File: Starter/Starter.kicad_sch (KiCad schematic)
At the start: 62 parts, among them J2 Speaker, J5 Conn_01x08_Pin, M1 Vibration Motor, Q1 2N2222, SW1 UP, SW2 LEFT, SW3 DOWN, SW4 RIGHT, U2 LP-MSPM0G3507, U3 MCP34119D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

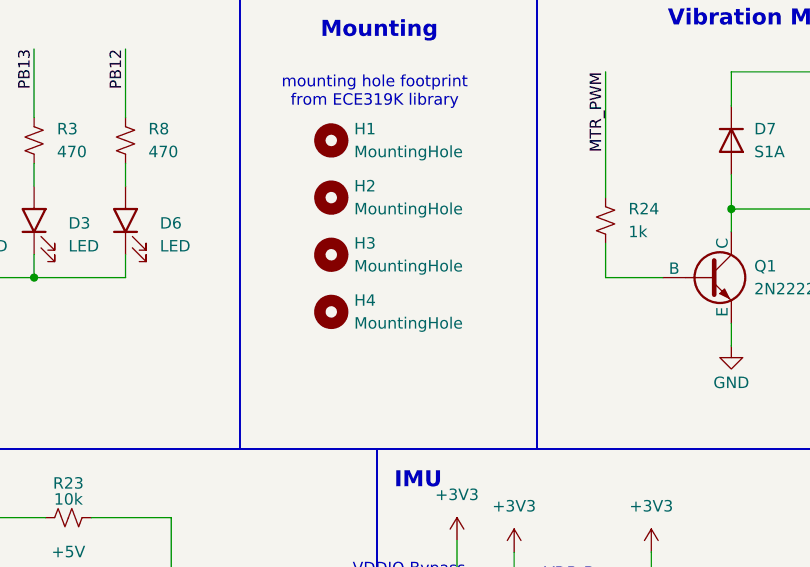
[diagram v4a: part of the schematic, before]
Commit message: Component placements finalized
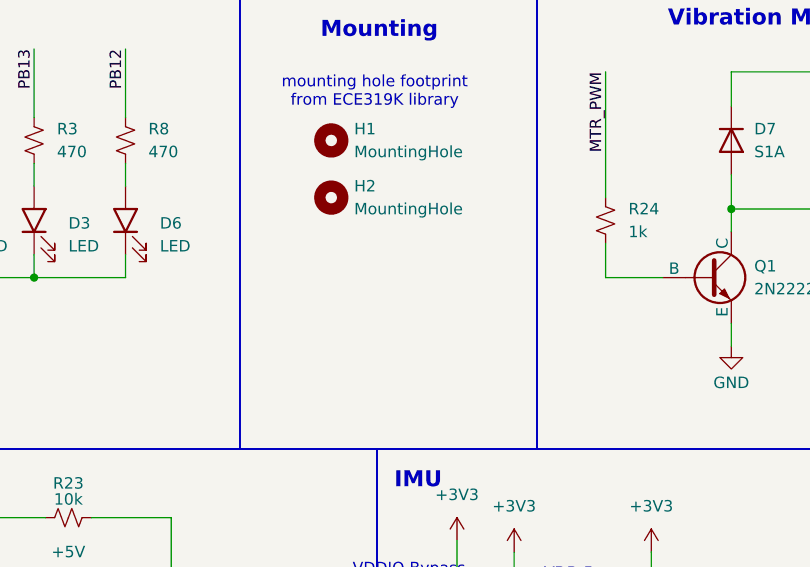
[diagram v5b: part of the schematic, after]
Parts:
- removed H3, H4: MountingHole, MountingHole:MountingHole_3.2mm_M3, symbol Mechanical:MountingHole
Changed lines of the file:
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@@
 	)
 	(symbol
-		(lib_id "Mechanical:MountingHole")
-		(at 261.62 156.21 0)
-		(unit 1)
-		(exclude_from_sim no)
-		(in_bom no)
-		(on_board yes)
-		(dnp no)
-		(fields_autoplaced yes)
-		(property "Reference" "H4"
-			(at 264.16 154.9399 0)
-			(effects
-				(font
-					(size 1.27 1.27)
-				)
-				(justify left)
-			)
-		)
-		(property "Value" "MountingHole"
-			(at 264.16 157.4799 0)
-			(effects
-				(font
-					(size 1.27 1.27)
-				)
-				(justify left)
-			)
-		)
-		(property "Footprint" "MountingHole:MountingHole_3.2mm_M3"
-			(at 261.62 156.21 0)
-			(effects
-				(font
-					(size 1.27 1.27)
-				)
-				(hide yes)
-			)
-		)
-		(property "Datasheet" "~"
-			(at 261.62 156.21 0)
-			(effects
-				(font
-					(size 1.27 1.27)
-				)
-				(hide yes)
-			)
-		)
-		(property "Description" "Mounting Hole without connection"
-			(at 261.62 156.21 0)
-			(effects
-				(font
-					(size 1.27 1.27)
-				)
-				(hide yes)
-			)
-		)
-		(property "Mouser Link" ""
-			(at 261.62 156.21 0)
-			(effects
-				(font
-					(size 1.27 1.27)
-				)
-				(hide yes)
-			)
-		)
-		(property "Mouser #" ""
-			(at 261.62 156.21 0)
-			(effects
-				(font
-					(size 1.27 1.27)
-				)
-				(hide yes)
-			)
-		)
-		(property "JLCPCB #" ""
-			(at 261.62 156.21 0)
-			(effects
-				(font
-					(size 1.27 1.27)
-				)
-				(hide yes)
-			)
-		)
-		(instances
-			(project "Starter"
-				(path "/69b823fd-c065-40ff-9bb9-c5835555f3eb"
-					(reference "H4")
-					(unit 1)
-				)
-			)
-		)
-	)
-	(symbol
 		(lib_id "ECE319K:C")
 		(at 212.09 205.74 270)
@@
 					(unit 1)
 				)
-			)
-		)
-	)
-	(symbol
-		(lib_id "Mechanical:MountingHole")
-		(at 261.62 149.86 0)
-		(unit 1)
-		(exclude_from_sim no)
-		(in_bom no)
-		(on_board yes)
-		(dnp no)
-		(fields_autoplaced yes)
-		(property "Reference" "H3"
-			(at 264.16 148.5899 0)
-			(effects
-				(font
-					(size 1.27 1.27)
-				)
-				(justify left)
-			)
-		)
-		(property "Value" "MountingHole"
-			(at 264.16 151.1299 0)
-			(effects
-				(font
-					(size 1.27 1.27)
-				)
-				(justify left)
-			)
-		)
-		(property "Footprint" "MountingHole:MountingHole_3.2mm_M3"
-			(at 261.62 149.86 0)
-			(effects
-				(font
-					(size 1.27 1.27)
-				)
-				(hide yes)
-			)
-		)
-		(property "Datasheet" "~"
-			(at 261.62 149.86 0)
-			(effects
-				(font
-					(size 1.27 1.27)
-				)
-				(hide yes)
-			)
-		)
-		(property "Description" "Mounting Hole without connection"
-			(at 261.62 149.86 0)
-			(effects
-				(font
-					(size 1.27 1.27)
-				)
-				(hide yes)
-			)
-		)
-		(property "Mouser Link" ""
-			(at 261.62 149.86 0)
-			(effects
-				(font
-					(size 1.27 1.27)
-				)
-				(hide yes)
-			)
-		)
-		(property "Mouser #" ""
-			(at 261.62 149.86 0)
-			(effects
-				(font
-					(size 1.27 1.27)
-				)
-				(hide yes)
-			)
-		)
-		(property "JLCPCB #" ""
-			(at 261.62 149.86 0)
-			(effects
-				(font
-					(size 1.27 1.27)
-				)
-				(hide yes)
-			)
-		)
-		(instances
-			(project "Starter"
-				(path "/69b823fd-c065-40ff-9bb9-c5835555f3eb"
-					(reference "H3")
-					(unit 1)
-				)

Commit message: final board! ordered
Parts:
- removed J5: Conn_01x08_Pin, Connector_PinSocket_2.54mm:PinSocket_1x08_P2.54mm_Vertical, symbol Connector:Conn_01x08_Pin
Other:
- note removed: "Extra"
- note removed: "break out any remaining pins here"

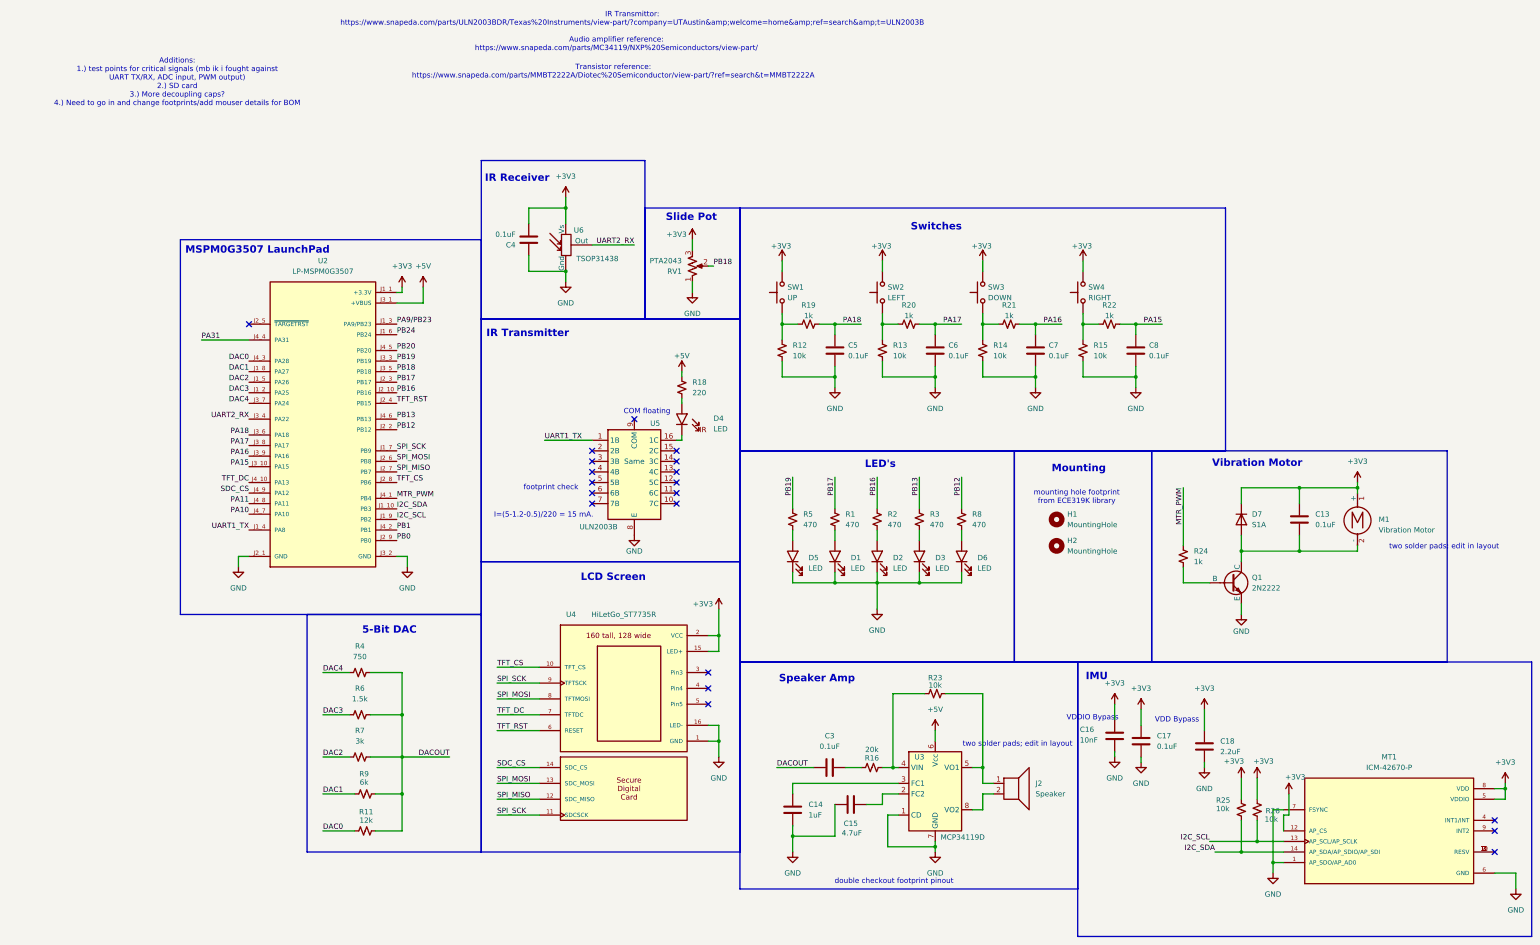
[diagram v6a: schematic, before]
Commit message: all mouser links attached
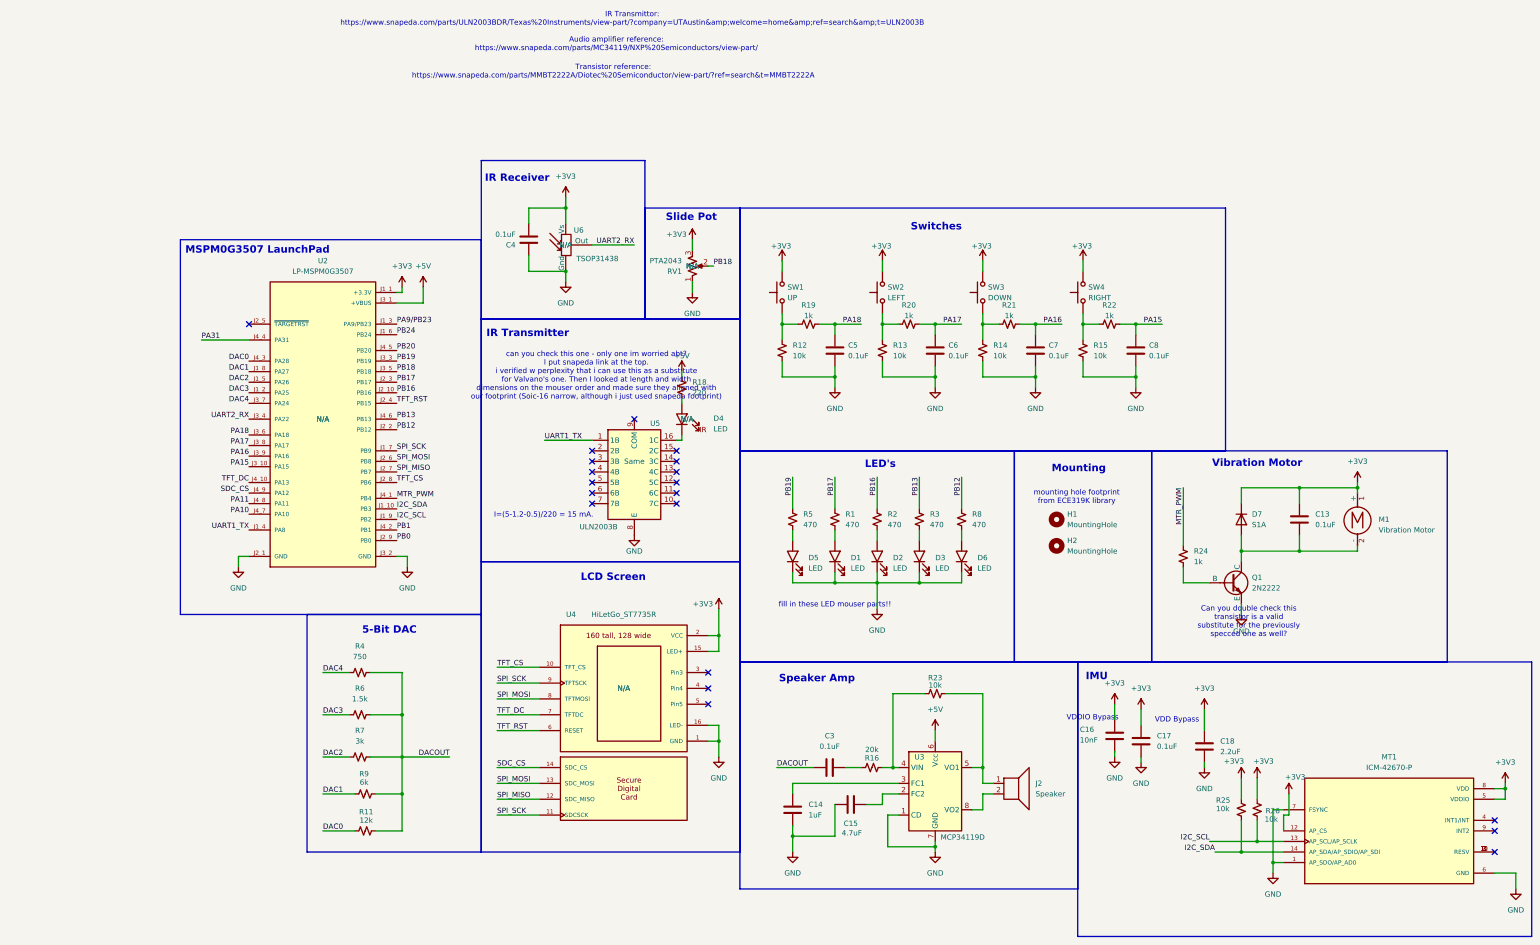
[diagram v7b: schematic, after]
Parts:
- C13, C17, C3, C4, C5, C6, C7, C8: Mouser # (none) -> 581-0603ZG104ZAT2A; Mouser Link (none) -> https://www.mouser.com/ProductDetail/KYOCERA-AVX/0603ZG104Z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
- C14: Mouser # (none) -> 963-LMK107B7105KA-T; Mouser Link (none) -> https://www.mouser.com/ProductDetail/TAIYO-YUDEN/LMK107B710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
- C15: Mouser # (none) -> 963-LMK107BJ475KA-T; Mouser Link (none) -> https://www.mouser.com/ProductDetail/TAIYO-YUDEN/LMK107BJ47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
- C16: Mouser # (none) -> 581-0603ZC103MAT2A; Mouser Link (none) -> https://www.mouser.com/ProductDetail/KYOCERA-AVX/0603ZC103M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
- C18: Mouser # (none) -> 963-LMK107BJ225KA-T; Mouser Link (none) -> https://www.mouser.com/ProductDetail/TAIYO-YUDEN/LMK107BJ22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
- D4, J2, RV1, U2, U3, U4, U6: Mouser # (none) -> N/A; Mouser Link (none) -> N/A
- M1: Mouser # 316040001 -> 713-316040001
- R1, R2, R3, R5, R8: Mouser # (none) -> 71-CRCW0603-470-E3; Mouser Link (none) -> https://www.mouser.com/ProductDetail/Vishay-Dale/CRCW060347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
- R11: Mouser # (none) -> 71-CRCW0603-12K-E3; Mouser Link (none) -> https://www.mouser.com/ProductDetail/Vishay-Dale/CRCW060312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
- R12, R13, R14, R15, R23, R25, R26: Mouser # (none) -> 71-CRCW060310K0FKEC; Mouser Link (none) -> https://www.mouser.com/ProductDetail/Vishay-Dale/CRCW060310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
- R16: Mouser # (none) -> 71-CRCW0603-20K-E3; Mouser Link (none) -> https://www.mouser.com/ProductDetail/Vishay-Dale/CRCW060320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
- R18: Mouser # (none) -> 71-CRCW0603-220-E3; Mouser Link (none) -> https://www.mouser.com/ProductDetail/Vishay-Dale/CRCW060322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
- R19, R20, R21, R22, R24: Mouser # (none) -> 71-CRCW06031K00FKEC; Mouser Link (none) -> https://www.mouser.com/ProductDetail/Vishay-Dale/CRCW06031K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
- R4: Mouser # (none) -> 71-CRCW0603-750-E3; Mouser Link (none) -> https://www.mouser.com/ProductDetail/Vishay-Dale/CRCW060375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
- R6: Mouser # (none) -> 71-CRCW06031K50FKEC; Mouser Link (none) -> https://www.mouser.com/ProductDetail/Vishay-Dale/CRCW06031K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
- R7: Mouser # (none) -> 71-CRCW0603-3K-E3; Mouser Link (none) -> https://www.mouser.com/ProductDetail/Vishay-Dale/CRCW06033K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
- R9: Mouser # (none) -> 71-CRCW0603-6.04K-E3; Mouser Link (none) -> https://www.mouser.com/ProductDetail/Vishay-Dale/CRCW06036K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
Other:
- note added: "Can you double check this transistor is a valid substitute for the previously specced one as well?"
- note added: "can you check this one - only one im worried abt? I put snapeda link at the top. i verified w perplexity that i can use this as a substitute for Valvano's one. Then I looked at length and width dimensions on the mouser order and made sure they aligned with our footprint (Soic-16 narrow, although i just used snapeda footprint)"
- note added: "fill in these LED mouser parts!!"
- note removed: "Additions: 1.) test points for critical signals (mb ik i fought against UART TX/RX, ADC input, PWM output) 2.) SD card 3.) More decoupling caps? 4.) Need to go in and change footprints/add mouser details for BOM"
- note removed: "COM floating"
- note removed: "double checkout footprint pinout"
- note removed: "footprint check"
- note removed: "two solder pads; edit in layout"

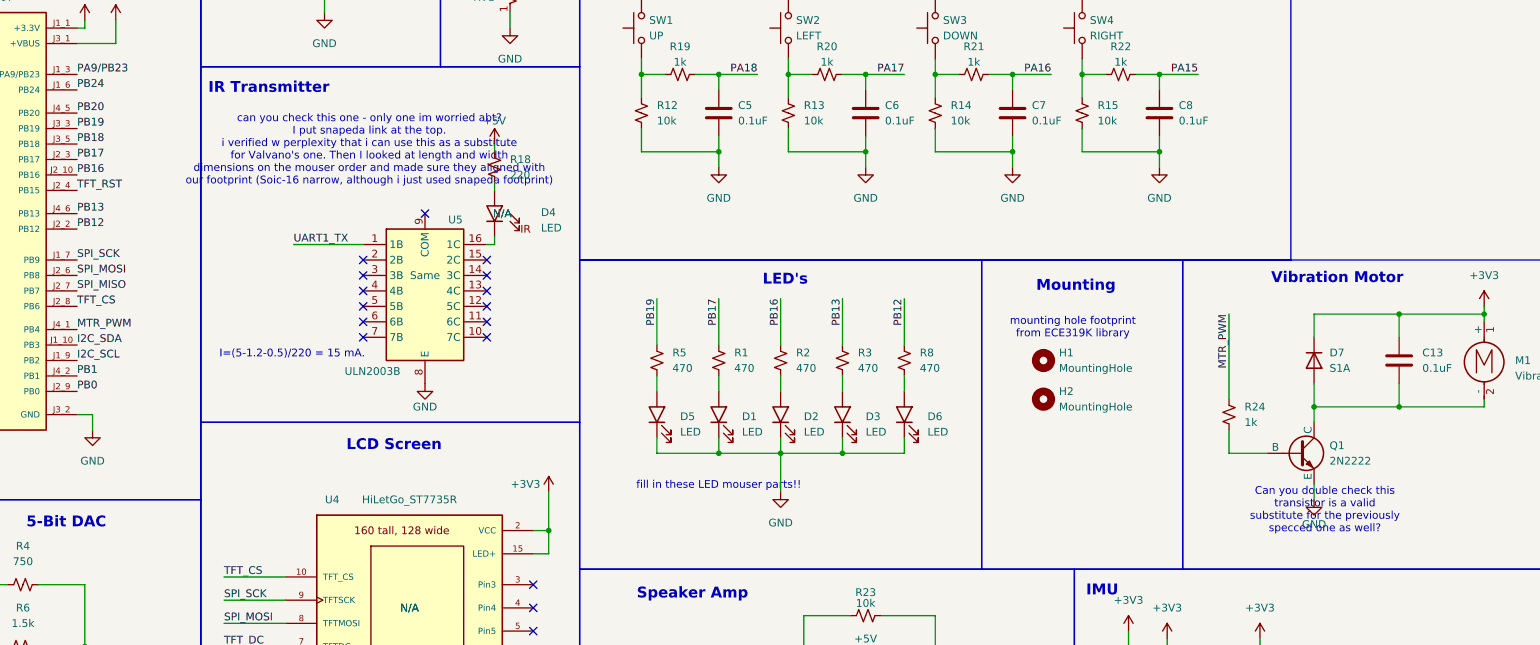
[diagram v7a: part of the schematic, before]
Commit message: added LED p/n
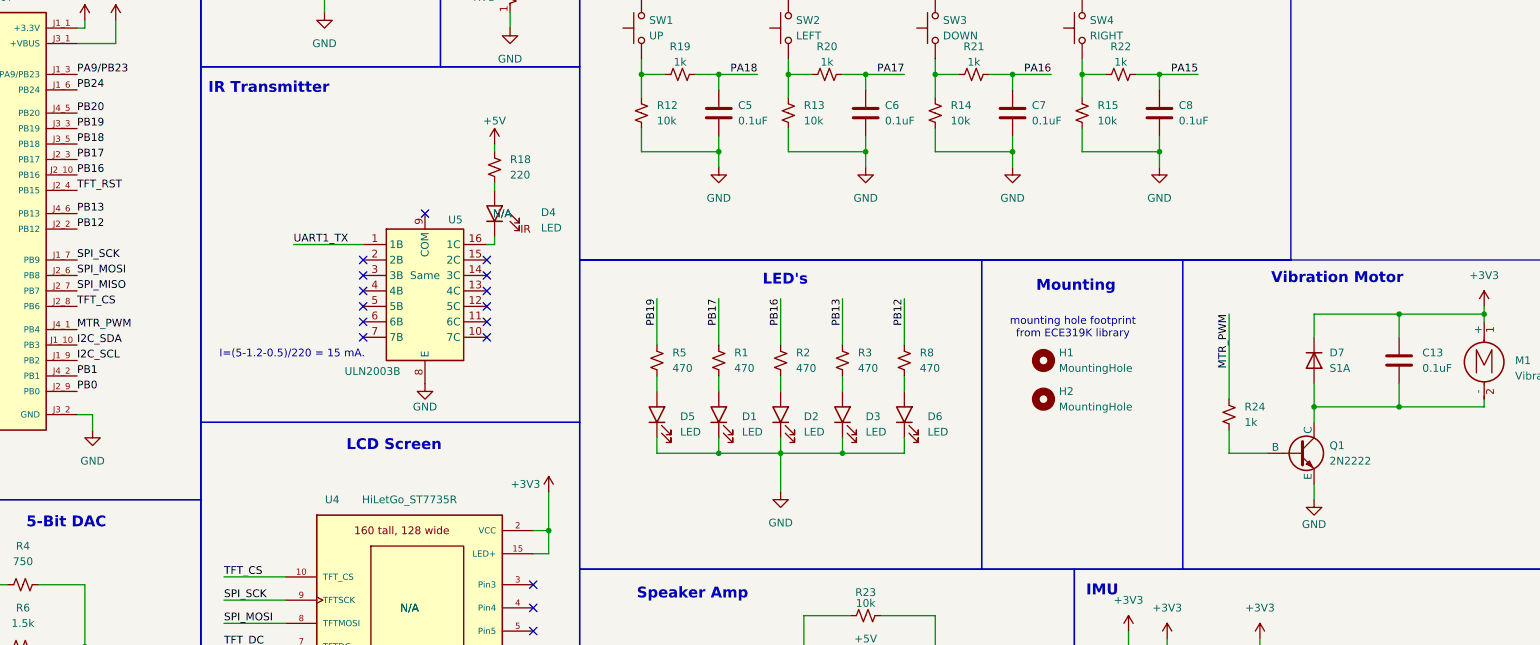
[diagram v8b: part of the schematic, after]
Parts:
- D1, D2, D3, D6: Mouser # (none) -> 604-APTD2012LCGCK; Mouser Link (none) -> https://www.mouser.com/ProductDetail/Kingbright/APTD2012LCG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
- D5: Mouser # (none) -> 604-APTD2012LCGCK
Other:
- note removed: "Can you double check this transistor is a valid substitute for the previously specced one as well?"
- note removed: "can you check this one - only one im worried abt? I put snapeda link at the top. i verified w perplexity that i can use this as a substitute for Valvano's one. Then I looked at length and width dimensions on the mouser order and made sure they aligned with our footprint (Soic-16 narrow, although i just used snapeda footprint)"
- note removed: "fill in these LED mouser parts!!"
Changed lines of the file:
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@@
 		)
 	)
-	(text "can you check this one - only one im worried abt?\nI put snapeda link at the top.\ni verified w perplexity that i can use this as a substitute\nfor Valvano's one. Then I looked at length and width\ndimensions on the mouser order and made sure they aligned with\nour footprint (Soic-16 narrow, although i just used snapeda footprint)"
-		(exclude_from_sim no)
-		(at 150.876 102.616 0)
-		(effects
-			(font
-				(size 1.27 1.27)
-				(color 255 10 43 1)
-			)
-		)
-	)
 	(text " I=(5-1.2-0.5)/220 = 15 mA."
 		(exclude_from_sim no)
@@
 		)
 	)
-	(text "fill in these LED mouser parts!!"
-		(exclude_from_sim no)
-		(at 208.28 157.734 0)
-		(effects
-			(font
-				(size 1.27 1.27)
-				(color 255 8 30 1)
-			)
-		)
-	)
-	(text "Can you double check this\ntransistor is a valid\nsubstitute for the previously\nspecced one as well?"
-		(exclude_from_sim no)
-		(at 307.848 161.798 0)
-		(effects
-			(font
-				(size 1.27 1.27)
-				(color 255 5 9 1)
-			)
-		)
-	)
 	(junction
 		(at 320.04 144.78)
@@
 			)
 		)
-		(property "Mouser Link" ""
+		(property "Mouser Link" "https://www.mouser.com/ProductDetail/Kingbright/APTD2012LCGCK?qs=AQlKX63v8RvNHN%2F9EGvNTg%3D%3D"
 			(at 229.87 146.05 0)
 			(effects
@@
 			)
 		)
-		(property "Mouser #" ""
+		(property "Mouser #" "604-APTD2012LCGCK "
 			(at 229.87 146.05 0)
 			(effects
@@
 			)
 		)
-		(property "Mouser Link" ""
+		(property "Mouser Link" "https://www.mouser.com/ProductDetail/Kingbright/APTD2012LCGCK?qs=AQlKX63v8RvNHN%2F9EGvNTg%3D%3D"
 			(at 219.71 146.05 0)
 			(effects
@@
 			)
 		)
-		(property "Mouser #" ""
+		(property "Mouser #" "604-APTD2012LCGCK "
 			(at 219.71 146.05 0)
 			(effects
@@
 			)
 		)
-		(property "Mouser Link" ""
+		(property "Mouser Link" "https://www.mouser.com/ProductDetail/Kingbright/APTD2012LCGCK?qs=AQlKX63v8RvNHN%2F9EGvNTg%3D%3D"
 			(at 240.03 146.05 0)
 			(effects
@@
 			)
 		)
-		(property "Mouser #" ""
+		(property "Mouser #" "604-APTD2012LCGCK "
 			(at 240.03 146.05 0)
 			(effects
@@
 			)
 		)
-		(property "Mouser Link" ""
+		(property "Mouser Link" "https://www.mouser.com/ProductDetail/Kingbright/APTD2012LCGCK?qs=AQlKX63v8RvNHN%2F9EGvNTg%3D%3D"
 			(at 209.55 146.05 0)
 			(effects
@@
 			)
 		)
-		(property "Mouser #" ""
+		(property "Mouser #" "604-APTD2012LCGCK "
 			(at 209.55 146.05 0)
 			(effects
@@
 			)
 		)
-		(property "Mouser #" ""
+		(property "Mouser #" "604-APTD2012LCGCK "
 			(at 199.39 146.05 0)
 			(effects
